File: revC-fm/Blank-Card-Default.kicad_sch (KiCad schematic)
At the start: 35 parts, among them J5 ZX62-AB-5PA(31), Q73 MUN5311DW1, SW4 EVQP7C01P, U25 AP2161W, U26 TVS0500DRV

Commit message: working
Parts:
- renumbered C86 to C67, C87 to C68, C88 to C69, C89 to C70, C90 to C71, C91 to C72, C92 to C73, C93 to C74, C94 to C75, C95 to C76, D6 to D10, D7 to D11, D2 to D6, D3 to D7, D4 to D8, D5 to D9, R138 to R110, R139 to R111, R140 to R112, R143 to R113, R144 to R114, R145 to R115, R146 to R116, R149 to R117, R150 to R118, U25 to U22, U26 to U23

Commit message: almost done!!!!!
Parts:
- C72: value 1nF -> 10nF
- R117: footprint Resistor_SMD:R_0402_1005Metric -> Resistor_SMD:R_0603_1608Metric
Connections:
- net STAT renamed USB_STAT
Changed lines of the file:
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@@
-    )
-  )
-  (global_label "STAT" (shape bidirectional) (at 181.61 120.65 180) (fields_autoplaced)
-    (effects (font (size 1.016 1.016)) (justify right))
-    (property "Intersheetrefs" "${INTERSHEET_REFS}" (at -29.21 7.62 0)
-      (effects (font (size 1.016 1.016)) hide)
-    )
-  )
-  (global_label "STAT" (shape bidirectional) (at 219.71 97.79 180) (fields_autoplaced)
-    (effects (font (size 1.016 1.016)) (justify right))
-    (property "Intersheetrefs" "${INTERSHEET_REFS}" (at 8.89 -15.24 0)
-      (effects (font (size 1.016 1.016)) hide)
     )
   )
@@
     )
   )
+  (global_label "USB_STAT" (shape input) (at 181.61 120.65 180) (fields_autoplaced)
+    (effects (font (size 1.016 1.016)) (justify right))
+    (property "Intersheetrefs" "${INTERSHEET_REFS}" (at 172.5999 120.65 0)
+      (effects (font (size 1.016 1.016)) (justify right) hide)
+    )
+  )
   (global_label "LED_PWR" (shape input) (at 146.05 85.09 180) (fields_autoplaced)
     (effects (font (size 1.016 1.016)) (justify right))
@@
     )
   )
+  (global_label "USB_STAT" (shape input) (at 219.71 97.79 180) (fields_autoplaced)
+    (effects (font (size 1.016 1.016)) (justify right))
+    (property "Intersheetrefs" "${INTERSHEET_REFS}" (at 210.6999 97.79 0)
+      (effects (font (size 1.016 1.016)) (justify right) hide)
+    )
+  )
   (symbol (lib_id "Device:R_US") (at 186.69 64.77 0) (unit 1)
     (in_bom yes) (on_board yes) (dnp no)
@@
       (effects (font (size 1.27 1.27)) (justify left))
     )
-    (property "Value" "1nF" (at 82.931 69.723 0)
+    (property "Value" "10nF" (at 82.931 69.723 0)
       (effects (font (size 1.27 1.27)) (justify left))
     )
@@
       (effects (font (size 1.27 1.27)) (justify left))
     )
-    (property "Footprint" "Resistor_SMD:R_0402_1005Metric" (at 134.366 161.544 90)
-      (effects (font (size 1.27 1.27)) hide)
-    )
+    (property "Footprint" "Resistor_SMD:R_0603_1608Metric" (at 134.366 161.544 90)
+      (effects (font (size 1.27 1.27)) hide)
+    )

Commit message: updated fab files
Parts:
- C120: renamed from C67; Manufacturer (none) -> TDK; Mfr. Part No (none) -> CGA2B3X7R1H104K050BE
- C121: renamed from C68; Manufacturer (none) -> TDK
- C122: renamed from C69; Manufacturer (none) -> TDK
- C123: renamed from C70; Manufacturer (none) -> TDK; Mfr. Part No (none) -> CGA2B3X7R1H104K050BE
- C124: renamed from C71; Manufacturer (none) -> TDK; Mfr. Part No (none) -> CGA2B3X7R1H104K050BE
- C125: renamed from C72; Manufacturer (none) -> TDK; Mfr. Part No (none) -> CGA2B3X7S2A103K050BB
- C126: renamed from C73; Manufacturer (none) -> TDK; Mfr. Part No (none) -> CGA2B3X7R1H104K050BE
- C127: renamed from C74; Manufacturer (none) -> TDK; Mfr. Part No (none) -> CGA2B3X7R1H104K050BE
- C128: renamed from C75; Manufacturer (none) -> TDK; Mfr. Part No (none) -> CGA2B3X7R1H104K050BE
- C129: renamed from C76; Manufacturer (none) -> TDK; Mfr. Part No (none) -> CGA2B3X7R1H104K050BE
- D11: renamed from D6; Manufacturer (none) -> Texas Instruments; Mfr. Part No (none) -> ESD321DPYR
- D12: renamed from D7; Manufacturer (none) -> Texas Instruments; Mfr. Part No (none) -> ESD321DPYR
- J5: Manufacturer (none) -> Hirose Electric; Mfr. Part No (none) -> ZX62-AB-5PA(31)
- LED10: renamed from D10; Manufacturer (none) -> Kingbright; Mfr. Part No APA2107SECK/J4-PRV -> APA2107SECK
- LED11: renamed from D11; Manufacturer (none) -> Kingbright; Mfr. Part No APA2107LSECK/J3-PRV -> APA2107LSECK
- LED8: renamed from D8; Manufacturer (none) -> Kingbright; Mfr. Part No APA2107SYCK/J3-PRV -> APA2107SYCK
- LED9: renamed from D9; Manufacturer (none) -> Kingbright
- Q73: Manufacturer (none) -> onsemi; Mfr. Part No (none) -> MUN5311DW1
- R262: renamed from R110; Manufacturer (none) -> Stackpole Electronics; Mfr. Part No (none) -> RMCF0402FT10K0
- R263: renamed from R111; Manufacturer (none) -> Stackpole Electronics; Mfr. Part No (none) -> RMCF0402FT10K0
- R264: renamed from R112; Manufacturer (none) -> Stackpole Electronics; Mfr. Part No (none) -> RMCF0402FT1M00
- R265: renamed from R113; Manufacturer (none) -> Stackpole Electronics; Mfr. Part No (none) -> RMCF0402FT1K50
- R266: renamed from R114; Manufacturer (none) -> Stackpole Electronics; Mfr. Part No (none) -> RMCF0402FT1K50
- R267: renamed from R115; Manufacturer (none) -> Stackpole Electronics; Mfr. Part No (none) -> RMCF0402FT1K50
- R268: renamed from R116; Manufacturer (none) -> Stackpole Electronics; Mfr. Part No (none) -> RMCF0402FT1K50
- R270: renamed from R118; Manufacturer (none) -> Stackpole Electronics; Mfr. Part No (none) -> RMCF0603ZT0R00
- SW4: Manufacturer (none) -> Panasonic
- U36: renamed from U22; Manufacturer (none) -> Diodes Incorporated
- U37: renamed from U23; Manufacturer (none) -> Vishay Siliconix
- renumbered R117 to R269

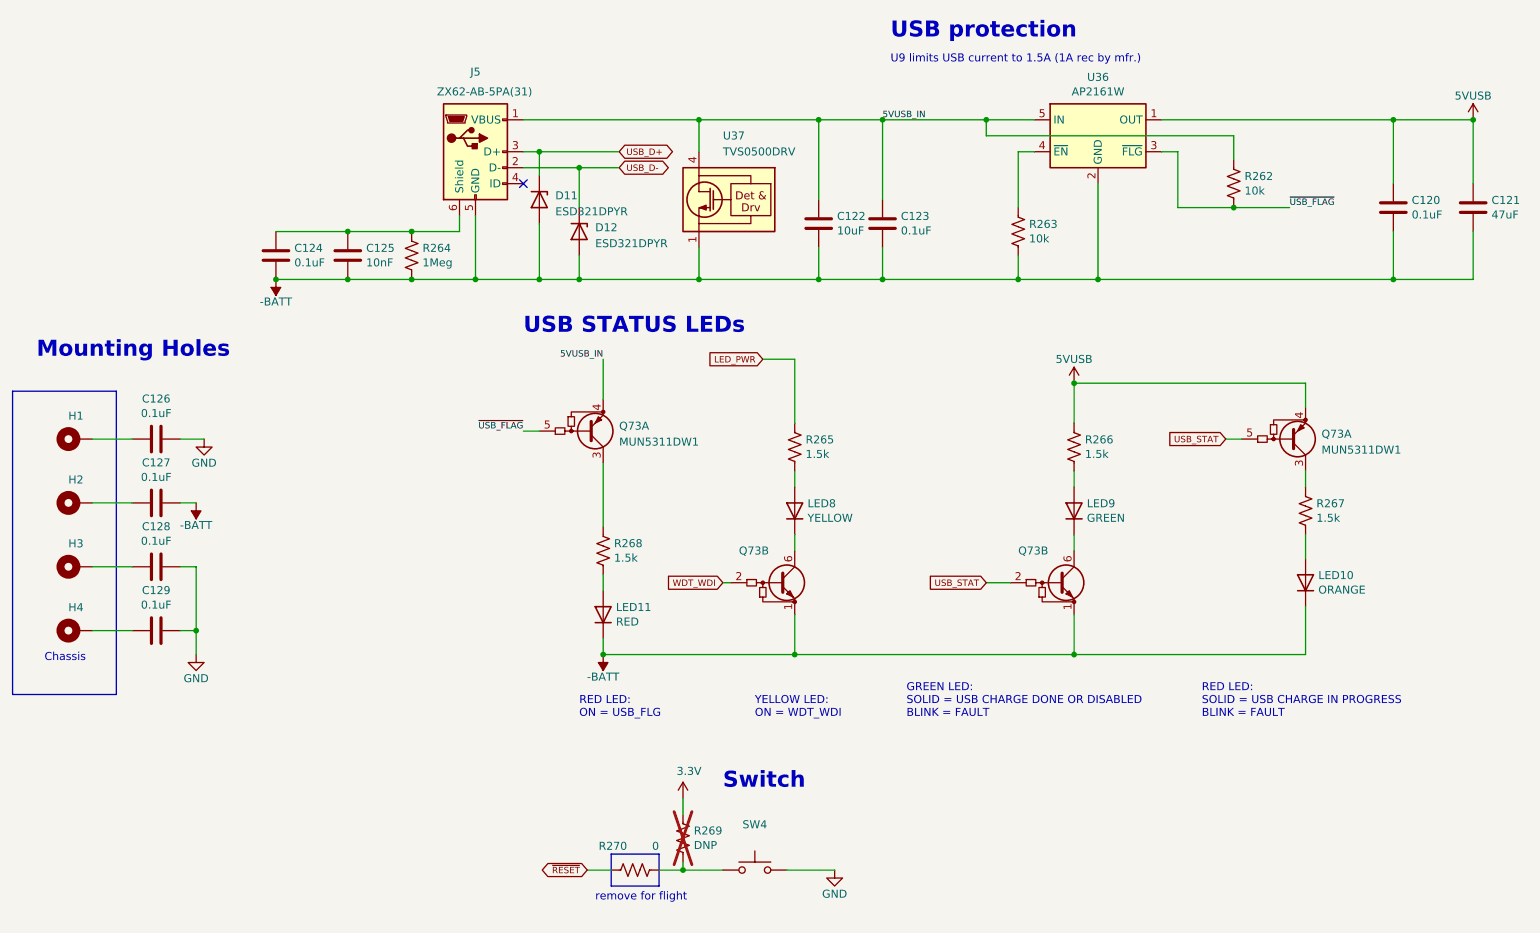
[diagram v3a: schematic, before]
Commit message: updated per review, improved docs
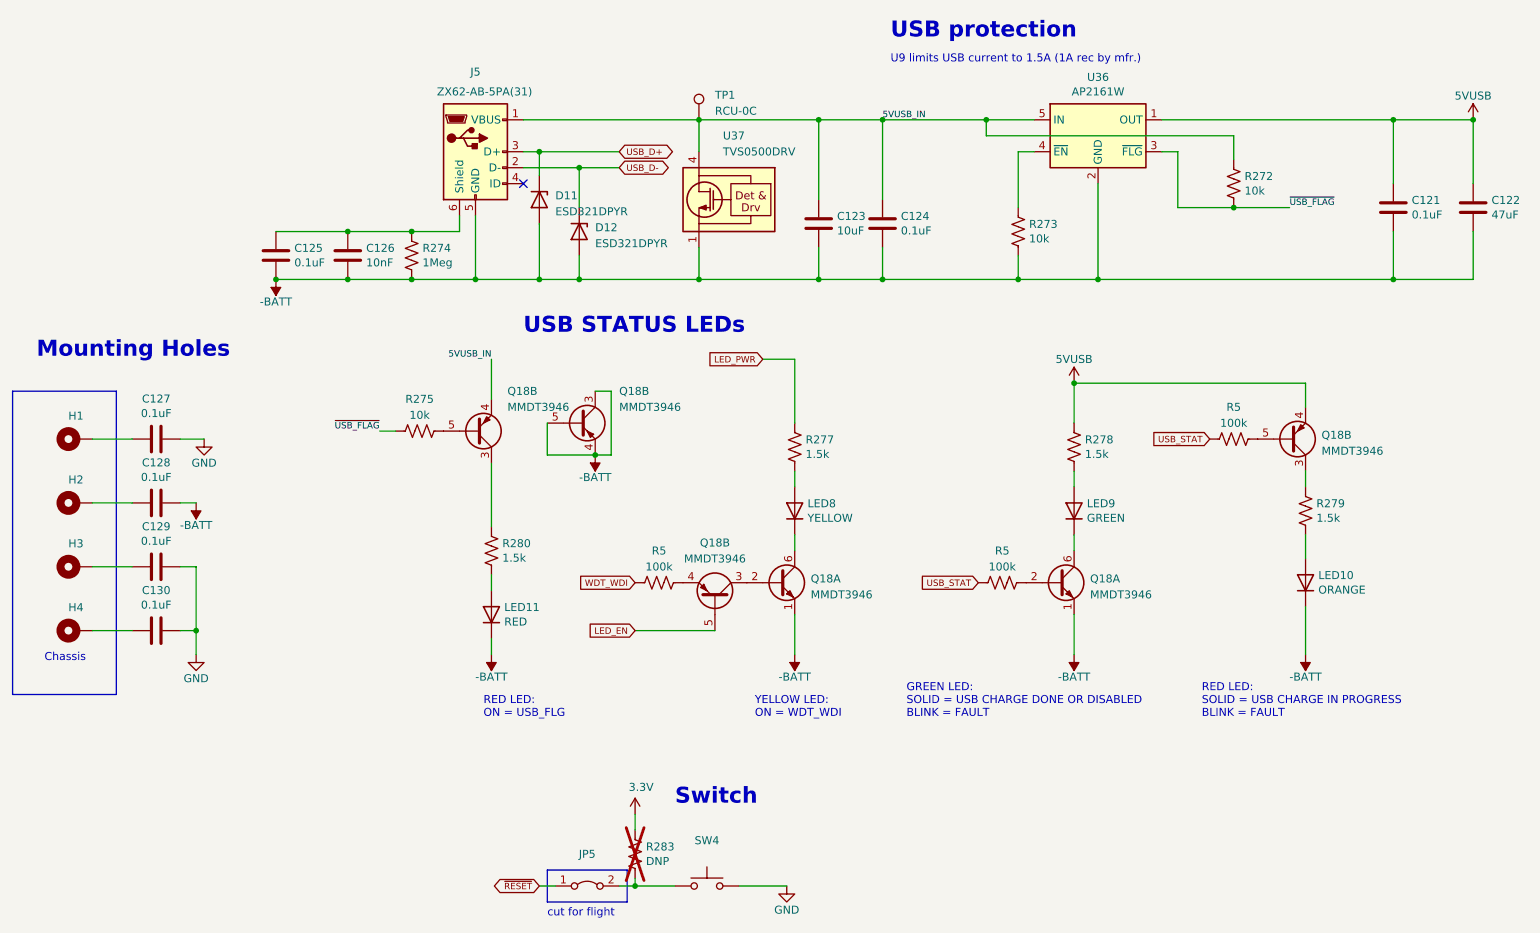
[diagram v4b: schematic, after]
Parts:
- removed Q73 (x2): MUN5311DW1, Package_TO_SOT_SMD:SOT-363_SC-70-6, symbol SierraLobo:MUN5312DW1
- removed R270: 0, Resistor_SMD:R_0603_1608Metric, symbol Device:R_US
- added JP5: Wire Cut Jumper, Resistor_SMD:R_0603_1608Metric, symbol Jumper:Jumper_2_Bridged
- added Q18 (x4): MMDT3946, Package_TO_SOT_SMD:SOT-363_SC-70-6, symbol Transistor_BJT:MMDT3946
- added R275: 10k, Resistor_SMD:R_0402_1005Metric, symbol Device:R_US
- added R5 (x3): 100k, Resistor_SMD:R_0402_1005Metric, symbol Device:R_US
- added TP1: RCU-0C, SierraLobo:TestPoint_TE_RCU_0603, symbol Connector:TestPoint
- R283: renamed from R269; Manufacturer (none) -> N/A; Mfr. Part No (none) -> N/A
- renumbered C120 to C121, C121 to C122, C122 to C123, C123 to C124, C124 to C125, C125 to C126, C126 to C127, C127 to C128, C128 to C129, C129 to C130, R262 to R272, R263 to R273, R264 to R274, R265 to R277, R266 to R278, R267 to R279, R268 to R280
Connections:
- net -BATT: now also Q18.1 (E1), Q18.1 (E1), Q18.3 (C2), Q18.4 (E2), Q18.5 (B2)
- net 5VUSB: now also Q18.4 (E2)
- net 5VUSB_IN: now also Q18.4 (E2), TP1.1
- net USB_STAT: now also R5.2, R5.2
- net WDT_WDI: now also R5.2
- net ~{RESET}: now also JP5.1 (A)
- net ~{USB_FLAG}: now also R275.1
- net at R280.1: now also Q18.3 (C2)
- net at LED8.1 (K): now also Q18.6 (C1)
- net at LED9.1 (K): now also Q18.6 (C1)
- net at R279.1: now also Q18.3 (C2)
- net at R283.2, SW4.1: now also JP5.2 (B)
- new net: Q18.4 (E2), R5.1
- new net: Q18.5 (B2), R5.1
- new net: Q18.5 (B2), R275.2
- new net: Q18.2 (B1), R5.1
- new net: Q18.2 (B1), Q18.3 (C2)
- new net LED_EN: Q18.5 (B2)
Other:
- note added: "cut for flight"
- note removed: "remove for flight"
- moved on the sheet: LED11, R280, R283, SW4
